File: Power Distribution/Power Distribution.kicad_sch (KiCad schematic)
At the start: 4 parts, among them SW1 SW_DPST_x2, U1 SC1176, U2 XL6009

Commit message: PCB
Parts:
- added C1, C2: C, symbol Device:C
- added LS1, LS2: Speaker, symbol Device:Speaker
- added P1: ChargingBoardTP4056, symbol ChargingBoardTP4056:ChargingBoardTP4056
- added R1, R2: R, symbol Device:R
- added U3: MCP4922, symbol Analog_DAC:MCP4922
- added U4: PAM8403D, Package_SO:SOP-16_3.9x9.9mm_P1.27mm, symbol Amplifier_Audio:PAM8403D
- added U5: 2472, 2472:MODULE_2472, symbol 2472:2472
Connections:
- net at BT1.1 (+), SW1.1 (A): now also P1.A4 (B+)
- net at U1.1 (3V3_1): now also U3.1 (Vdd), U3.10 (VB), U3.11 (VrefB), U3.13 (VrefA), U4.10 (INR), U4.6 (VDD), U4.8 (VREF), U5.1 (VIN)
- net at U1.27 (ID_SD): now also U3.5 (SDI)
- net at U1.28 (ID_SC): now also U3.4 (SCK)
- net at U1.29 (GPIO5): now also U5.5 (SCL)
- net at U1.6 (GND_6), U2.4 (-VDC): now also U5.3 (GND)
- net at U1.7 (GPIO4/GPIO_GCLK): now also U5.4 (SDA)
- net at BT1.2 (-), U2.2 (+VDC), U2.8 (VIN-): now also P1.A3 (B+)
- new net: R1.1, U4.1 (LOUT+)
- new net: R2.1, U4.14 (ROUT-)
- new net: LS2.2, U4.16 (ROUT+)
- new net: LS1.2, U4.3 (LOUT-)
- new net: U3.14 (VA), U4.7 (INL)
- new net: C2.1, LS2.1, R2.2
- new net: C1.1, LS1.1, R1.2
- new net: P1.A1 (Vout+), P1.A9 (VBUS), P1.B4 (VBUS), P1.B9 (VBUS)
- new net GND: C1.2, C2.2, U3.12 (Vss), U4.11 (GND), U4.13 (PVDD), U4.15 (PGND), U4.2 (PGND), U4.4 (PVDD)
- no-connect marks 0 -> 40
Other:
- moved on the sheet: BT1, U1

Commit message: updated the schematic for PCB
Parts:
- BT1: value Battery_Cell -> LiPo (LPLP103454)
- P1: footprint (none) -> ChargingBoardTP4056:Charging Board TP4056
- SW1: value SW_DPST_x2 -> Switch
- U1: value SC1176 -> Raspberry Pi Zero 2 W
- U2: value XL6009 -> Charging Board XL6009; footprint XL6009 Module DC-DC -> XL6009:XL6009
- U3: value MCP4922 -> DAC MCP4922
- U4: value PAM8403D -> Audio Ampifier PAM8403D
- U5: value 2472 -> IMU BNO55
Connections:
- net at U1.1 (3V3_1), U3.1 (Vdd), U3.11 (VrefB)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: no longer U3.10 (VB), U4.10 (INR)
- new net: U3.10 (VB), U4.10 (INR)
- no-connect marks 40 -> 42
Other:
- note added: "3.3V"
- note added: "3.7V"
- note added: "4.2V"
- note added: "5V"
- note added: "GND"
- moved on the sheet: C1, C2, LS1, LS2, R1, R2

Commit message: Updated the PCB schematic
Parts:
- removed C1, C2: C, symbol Device:C
- removed R1, R2: R, symbol Device:R
- added C1: 47uF, 47uF:CAPC3225X280N, symbol GCJ32ER70J476KE01L:GCJ32ER70J476KE01L
- added C2, C3, C4, C5, C6, C7: 47nF, 47nf:CAP_PAN_EEE_K16_PAN-L, symbol 2025-03-19_20-04-15:EEV-TG1A472M
- added R1: 47kΩ, 47k:RES_ERA6ARW473V, symbol ERA6ARW473V:ERA6ARW473V
- added R2, R3, R4, R5, R6, R7: 1kΩ, 1k:RES_ERJ2RKF1001X, symbol ERJ2RKF1001X:ERJ2RKF1001X
- added U6: DM-OLED096-636, OLED:MODULE_DM-OLED096-636, symbol DM-OLED096-636:DM-OLED096-636
- renumbered BT1 to Battery
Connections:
- net GND: now also C2.2, C3.2, C5.2, C6.2, R4.1, R7.1, U6.1 (GND)
- net at Battery.2 (-), P1.A3 (B+), U2.2 (+VDC)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: now also C1.1
- net at U2.1 (VIN+), U2.6 (VIN+): now also C1.2, R1.2; no longer SW1.2 (B)
- net at U3.1 (Vdd), U3.11 (VrefB), U3.13 (VrefA)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: no longer U1.1 (3V3_1), U5.1 (VIN)
- net at U1.19 (GPIO10/SPI_MOSI): now also U3.5 (SDI)
- net at U1.2 (5V_2), U2.2 (+VDC), U2.3 (+VDC): now also U1.1 (3V3_1), U1.4 (5V_4), U5.1 (VIN), U6.2 (VCC_IN)
- net at U1.23 (GPIO11/SPI_SCLK): now also U3.4 (SCK)
- net at U1.26 (GPIO7/SPI_~{CE1}): now also U3.3 (~{CS})
- net at U1.27 (ID_SD): now also U5.4 (SDA); no longer U3.5 (SDI)
- net at U1.28 (ID_SC): now also U5.5 (SCL); no longer U3.4 (SCK)
- net at U1.29 (GPIO5): no longer U5.5 (SCL)
- net at U1.3 (GPIO2/SDA1): now also U6.4 (SDA)
- net at U1.5 (GPIO3/SCL): now also U6.3 (SCL)
- net at U1.7 (GPIO4/GPIO_GCLK): no longer U5.4 (SDA)
- net at U4.1 (LOUT+): now also LS1.1
- net at U4.10 (INR): now also C7.2, R7.2; no longer U3.10 (VB)
- net at U4.14 (ROUT-): now also LS2.1
- net at U4.7 (INL): now also C4.2, R4.2; no longer U3.14 (VA)
- new net: C5.1, R5.2, R6.1
- new net: C6.1, C7.1, R6.2
- new net: R1.1, SW1.2 (B)
- new net: C3.1, C4.1, R3.2
- new net: R2.1, U3.10 (VB)
- new net: R5.1, U3.14 (VA)
- new net: C2.1, R2.2, R3.1
- no-connect marks 42 -> 41
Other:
- note added: "13.3V"
- company: (none) -> VISION
- title: (none) -> Proposed Power Distribution Schematics
- moved on the sheet: LS1, LS2

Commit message: PCB in progress
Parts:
- removed C2, C3, C4, C5, C6, C7: 47nF, 47nf:CAP_PAN_EEE_K16_PAN-L, symbol 2025-03-19_20-04-15:EEV-TG1A472M
- removed LS1, LS2: Speaker, symbol Device:Speaker
- removed R2, R3, R4, R5, R6, R7: 1kΩ, 1k:RES_ERJ2RKF1001X, symbol ERJ2RKF1001X:ERJ2RKF1001X
- removed U2: Charging Board XL6009, XL6009:XL6009, symbol XL6009:XL6009
- removed U3: DAC MCP4922, symbol Analog_DAC:MCP4922
- removed U4: Audio Ampifier PAM8403D, Package_SO:SOP-16_3.9x9.9mm_P1.27mm, symbol Amplifier_Audio:PAM8403D
- removed U6: DM-OLED096-636, OLED:MODULE_DM-OLED096-636, symbol DM-OLED096-636:DM-OLED096-636
- U1: footprint SC1176:MODULE_SC1176 -> Raspberry Pi Zero 2 w:MODULE_SC1176
- renumbered Battery to Battery1
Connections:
- net at P1.A1 (Vout+), P1.A9 (VBUS), P1.B4 (VBUS)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: now also SW1.1 (A)
- net at P1.A2 (Vout-): now also C1.1, U1.6 (GND_6), U5.3 (GND)
- net at C1.2, R1.2: now also U1.1 (3V3_1), U1.2 (5V_2), U1.4 (5V_4), U5.1 (VIN)
- new net: Battery1.1 (+), P1.A3 (B+)
- new net: Battery1.2 (-), P1.A4 (B-)
- no-connect marks 41 -> 38
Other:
- note removed: "3.7V"
- moved on the sheet: Battery1, C1, R1

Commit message: Updated the PCB
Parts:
- added RPI1: ~, Adafruit 128x32 Pi OLED:RASPBERRYPI_2X3, symbol Adafruit 128x32 Pi OLED-eagle-import:RASPBERRYPI_2X3_THM
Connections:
- net GND: now also RPI1.6 (GND)
- net at C1.2, R1.2, U1.2 (5V_2): now also RPI1.2 (+5V), RPI1.4 (+5V); no longer U1.1 (3V3_1), U1.4 (5V_4), U5.1 (VIN)
- net at U1.3 (GPIO2/SDA1): now also RPI1.5 (SDA)
- net at U1.5 (GPIO3/SCL): now also RPI1.3 (SCL)
- new net: RPI1.1 (3.3V), U1.1 (3V3_1), U5.1 (VIN)
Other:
- note removed: "13.3V"
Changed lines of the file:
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@@
 		(company "VISION")
-	)
-	(text "13.3V"
-		(exclude_from_sim no)
-		(at 125.73 41.402 0)
-		(effects
-			(font
-				(size 1.27 1.27)
-			)
-		)
 	)
 	(text "GND\n"
@@
 	)
 	(junction
-		(at 218.44 41.91)
-		(diameter 0)
-		(color 0 0 0 0)
-	)
-	(junction
-		(at 142.24 41.91)
-		(diameter 0)
-		(color 0 0 0 0)
-	)
-	(junction
-		(at 139.7 41.91)
+		(at 142.24 35.56)
 		(diameter 0)
 		(color 0 0 0 0)
@@
 	)
 	(junction
-		(at 137.16 41.91)
+		(at 218.44 41.91)
 		(diameter 0)
 		(color 0 0 0 0)
@@
 	(wire
 		(pts
-			(xy 139.7 26.67) (xy 139.7 41.91)
-		)
-		(stroke
-			(width 0)
-			(type default)
-		)
-	)
-	(wire
-		(pts
 			(xy 217.17 116.84) (xy 217.17 90.17)
 		)
@@
 	(wire
 		(pts
-			(xy 124.46 46.99) (xy 137.16 46.99)
+			(xy 114.3 26.67) (xy 218.44 26.67)
 		)
 		(stroke
@@
 	(wire
 		(pts
-			(xy 218.44 25.4) (xy 137.16 25.4)
+			(xy 142.24 27.94) (xy 210.82 27.94)
 		)
 		(stroke
@@
 	(wire
 		(pts
-			(xy 137.16 41.91) (xy 139.7 41.91)
-		)
-		(stroke
-			(width 0)
-			(type default)
-		)
-	)
-	(wire
-		(pts
 			(xy 210.82 41.91) (xy 218.44 41.91)
 		)
@@
 	(wire
 		(pts
-			(xy 210.82 39.37) (xy 214.63 39.37)
-		)
-		(stroke
-			(width 0)
-			(type default)
-		)
-	)
-	(wire
-		(pts
 			(xy 220.98 63.5) (xy 222.25 63.5)
 		)
@@
 	(wire
 		(pts
-			(xy 137.16 25.4) (xy 137.16 41.91)
-		)
-		(stroke
-			(width 0)
-			(type default)
-		)
-	)
-	(wire
-		(pts
-			(xy 147.32 53.34) (xy 147.32 52.07)
-		)
-		(stroke
-			(width 0)
-			(type default)
-		)
-	)
-	(wire
-		(pts
 			(xy 142.24 78.74) (xy 142.24 116.84)
 		)
@@
 	(wire
 		(pts
+			(xy 142.24 35.56) (xy 142.24 27.94)
+		)
+		(stroke
+			(width 0)
+			(type default)
+		)
+	)
+	(wire
+		(pts
 			(xy 210.82 36.83) (xy 210.82 27.94)
 		)
@@
 	(wire
 		(pts
-			(xy 142.24 27.94) (xy 142.24 41.91)
-		)
-		(stroke
-			(width 0)
-			(type default)
-		)
-	)
-	(wire
-		(pts
 			(xy 149.86 111.76) (xy 218.44 111.76)
 		)
@@
 	(wire
 		(pts
-			(xy 218.44 41.91) (xy 218.44 25.4)
-		)
-		(stroke
-			(width 0)
-			(type default)
-		)
-	)
-	(wire
-		(pts
-			(xy 137.16 46.99) (xy 137.16 53.34)
-		)
-		(stroke
-			(width 0)
-			(type default)
-		)
-	)
-	(wire
-		(pts
 			(xy 143.51 115.57) (xy 220.98 115.57)
 		)
@@
 	(wire
 		(pts
-			(xy 142.24 41.91) (xy 142.24 71.12)
+			(xy 142.24 35.56) (xy 142.24 71.12)
 		)
 		(stroke
@@
 	(wire
 		(pts
-			(xy 124.46 41.91) (xy 137.16 41.91)
+			(xy 111.76 40.64) (xy 111.76 52.07)
 		)
 		(stroke
@@
 	(wire
 		(pts
-			(xy 124.46 49.53) (xy 149.86 49.53)
+			(xy 113.03 49.53) (xy 149.86 49.53)
+		)
+		(stroke
+			(width 0)
+			(type default)
+		)
+	)
+	(wire
+		(pts
+			(xy 111.76 52.07) (xy 149.86 52.07)
 		)
 		(stroke
@@
 	(wire
 		(pts
-			(xy 139.7 41.91) (xy 142.24 41.91)
-		)
-		(stroke
-			(width 0)
-			(type default)
-		)
-	)
-	(wire
-		(pts
-			(xy 137.16 53.34) (xy 147.32 53.34)
-		)
-		(stroke
-			(width 0)
-			(type default)
-		)
-	)
-	(wire
-		(pts
-			(xy 214.63 39.37) (xy 214.63 26.67)
-		)
-		(stroke
-			(width 0)
-			(type default)
-		)
-	)
-	(wire
-		(pts
-			(xy 147.32 52.07) (xy 149.86 52.07)
-		)
-		(stroke
-			(width 0)
-			(type default)
-		)
-	)
-	(wire
-		(pts
-			(xy 210.82 27.94) (xy 142.24 27.94)
+			(xy 114.3 40.64) (xy 111.76 40.64)
+		)
+		(stroke
+			(width 0)
+			(type default)
+		)
+	)
+	(wire
+		(pts
+			(xy 218.44 26.67) (xy 218.44 41.91)
+		)
+		(stroke
+			(width 0)
+			(type default)
+		)
+	)
+	(wire
+		(pts
+			(xy 113.03 38.1) (xy 113.03 49.53)
+		)
+		(stroke
+			(width 0)
+			(type default)
+		)
+	)
+	(wire
+		(pts
+			(xy 114.3 38.1) (xy 113.03 38.1)
+		)
+		(stroke
+			(width 0)
+			(type default)
+		)
+	)
+	(wire
+		(pts
+			(xy 139.7 35.56) (xy 142.24 35.56)
 		)
 		(stroke
@@
 	(wire
 		(pts
-			(xy 214.63 26.67) (xy 139.7 26.67)
+			(xy 114.3 35.56) (xy 114.3 26.67)
 		)
 		(stroke
@@
 	)
 	(symbol
+		(lib_id "Adafruit 128x32 Pi OLED-eagle-import:RASPBERRYPI_2X3_THM")
+		(at 127 38.1 0)
+		(unit 1)
+		(exclude_from_sim no)
+		(in_bom yes)
+		(on_board yes)
+		(dnp no)
+		(fields_autoplaced yes)
+		(property "Reference" "RPI1"
+			(at 127 38.1 0)
+			(effects
+				(font
+					(size 1.27 1.27)
+				)
+				(hide yes)
+			)
+		)
+		(property "Value" "~"
+			(at 127 38.1 0)
+			(effects
+				(font
+					(size 1.27 1.27)
+				)
+				(hide yes)
+			)
+		)
+		(property "Footprint" "Adafruit 128x32 Pi OLED:RASPBERRYPI_2X3"
+			(at 127 38.1 0)
+			(effects
+				(font
+					(size 1.27 1.27)
+				)
+				(hide yes)
+			)
+		)
+		(property "Datasheet" ""
+			(at 127 38.1 0)
+			(effects
+				(font
+					(size 1.27 1.27)
+				)
+				(hide yes)
+			)
+		)
+		(property "Description" ""
+			(at 127 38.1 0)
+			(effects
+				(font
+					(size 1.27 1.27)
+				)
+				(hide yes)
+			)
+		)
+		(pin "2"
+		)
+		(pin "1"
+		)
+		(pin "5"
+		)
+		(pin "3"
+		)
+		(pin "4"
+		)
+		(pin "6"
+		)
+		(instances
+			(project ""
+				(path "/ec1b8d42-e234-41e0-8bcf-2b2f52e7d9b3"
+					(reference "RPI1")
+					(unit 1)
+				)
+			)
+		)
+	)
+	(symbol
 		(lib_id "Switch:SW_DPST_x2")
 		(at 116.84 71.12 0)
@@
 	(symbol
 		(lib_id "power:Earth")
-		(at 124.46 54.61 0)
+		(at 139.7 40.64 0)
 		(unit 1)
 		(exclude_from_sim no)
@@
 		(fields_autoplaced yes)
 		(property "Reference" "#PWR010"
-			(at 124.46 60.96 0)
+			(at 139.7 46.99 0)
 			(effects
 				(font
@@
 		)
 		(property "Value" "GND"
-			(at 124.46 59.69 0)
+			(at 139.7 45.72 0)
 			(effects
 				(font
@@
 		)
 		(property "Footprint" ""
-			(at 124.46 54.61 0)
+			(at 139.7 40.64 0)
 			(effects
 				(font
@@
 		)
 		(property "Datasheet" "~"
-			(at 124.46 54.61 0)
+			(at 139.7 40.64 0)
 			(effects
 				(font
@@
 		)
 		(property "Description" "Power symbol creates a global label with name \"Earth\""
-			(at 124.46 54.61 0)
-			(effects
-				(font
+			(at 139.7 40.64 0)
+			(effects
+				(font

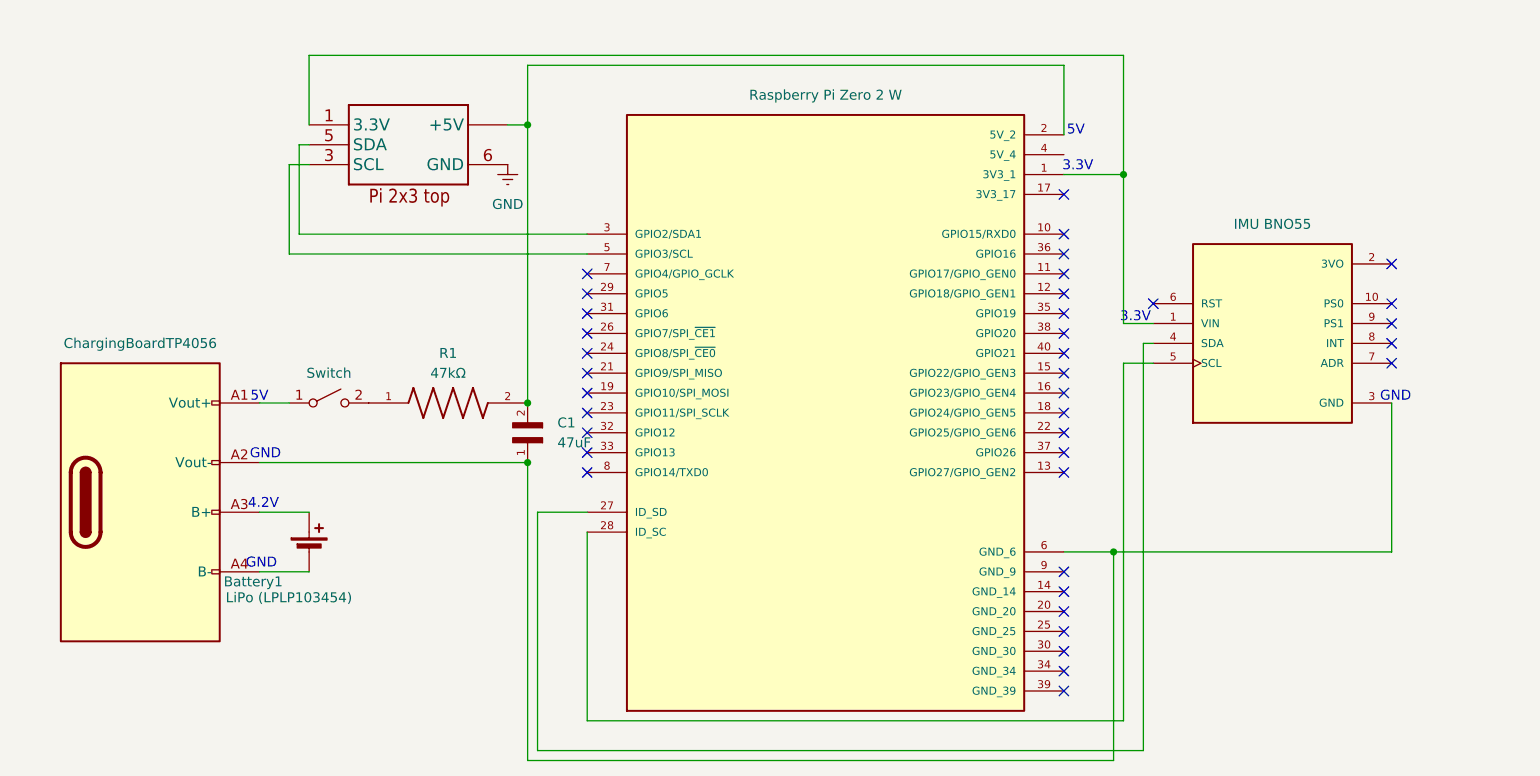
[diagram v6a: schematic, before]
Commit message: Finish adding the PCM5102a DAC Decoder
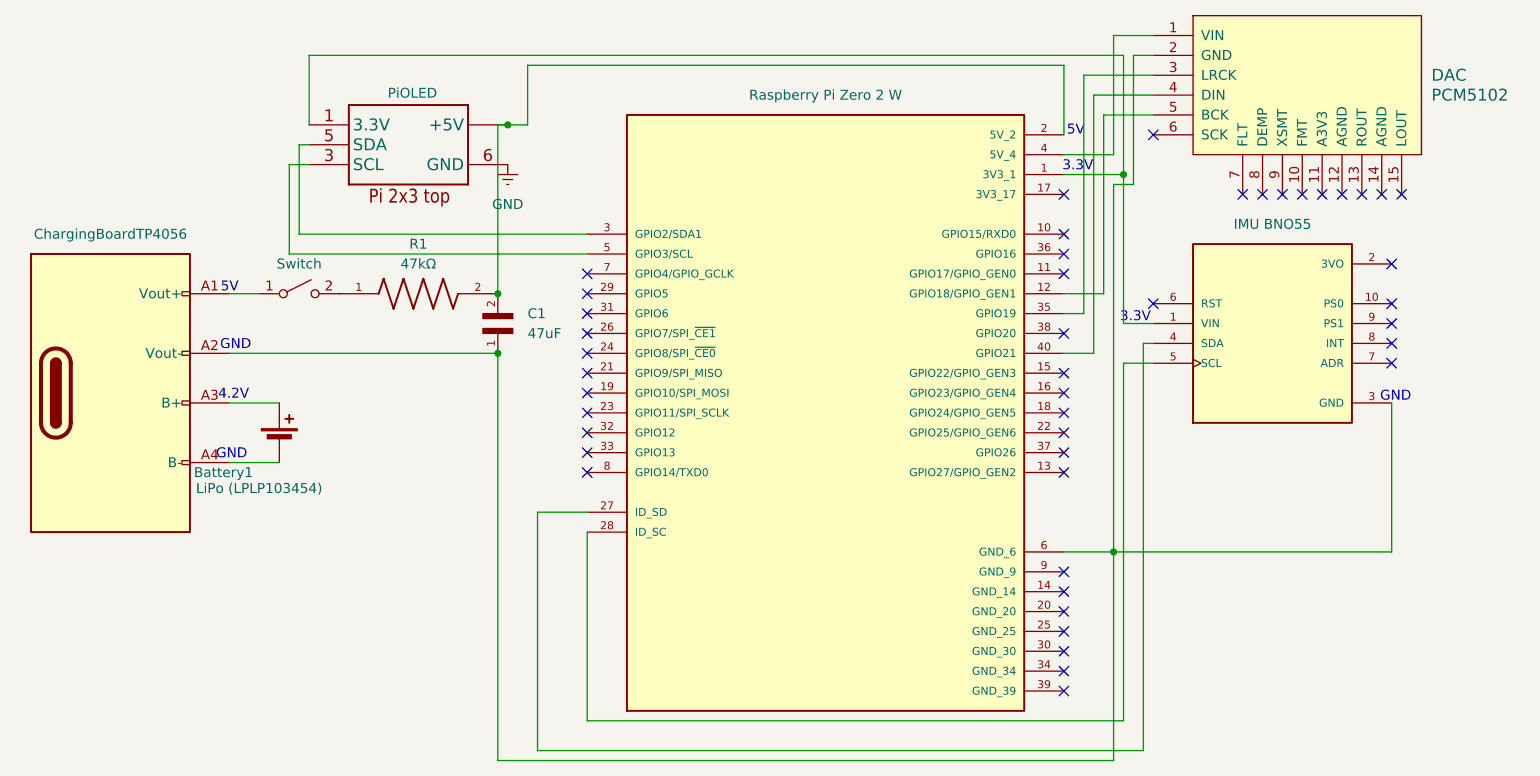
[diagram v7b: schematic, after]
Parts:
- added DAC: PCM5102, PCM5102:PCM5102, symbol comp_pcm5102:PCM5102
- renumbered RPI1 to PiOLED
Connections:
- net at C1.1, P1.A2 (Vout-), U1.6 (GND_6)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: now also DAC.2 (GND)
- net at U1.12 (GPIO18/GPIO_GEN1): now also DAC.5 (BCK)
- net at U1.35 (GPIO19): now also DAC.3 (LRCK)
- net at U1.4 (5V_4): now also DAC.1 (VIN)
- net at U1.40 (GPIO21): now also DAC.4 (DIN)
- no-connect marks 38 -> 45
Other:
- moved on the sheet: Battery1, C1, R1

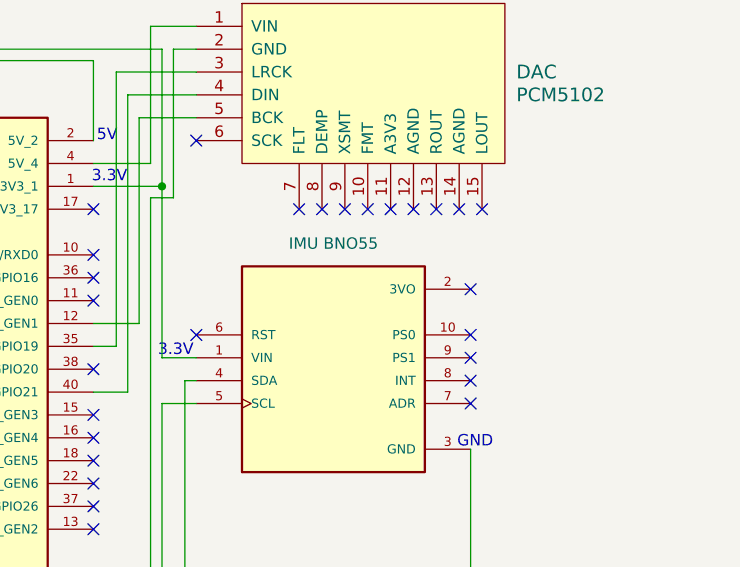
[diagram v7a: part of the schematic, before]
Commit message: added the speaker
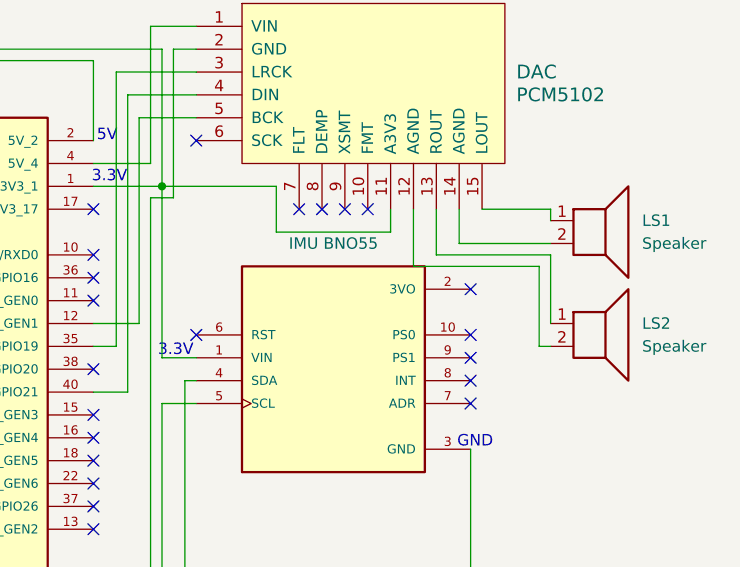
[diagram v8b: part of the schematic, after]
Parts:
- added LS1, LS2: Speaker, symbol Device:Speaker
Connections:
- net at PiOLED.1 (3.3V), U1.1 (3V3_1), U5.1 (VIN): now also DAC.11 (A3V3)
- net at DAC.12 (AGND): now also LS2.2
- net at DAC.13 (ROUT): now also LS2.1
- net at DAC.14 (AGND): now also LS1.2
- net at DAC.15 (LOUT): now also LS1.1
- no-connect marks 45 -> 40
